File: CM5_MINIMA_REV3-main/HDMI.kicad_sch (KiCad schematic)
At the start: 7 parts, among them J501 GT-HD001B-CNNG1, U405 STMPS2151STR

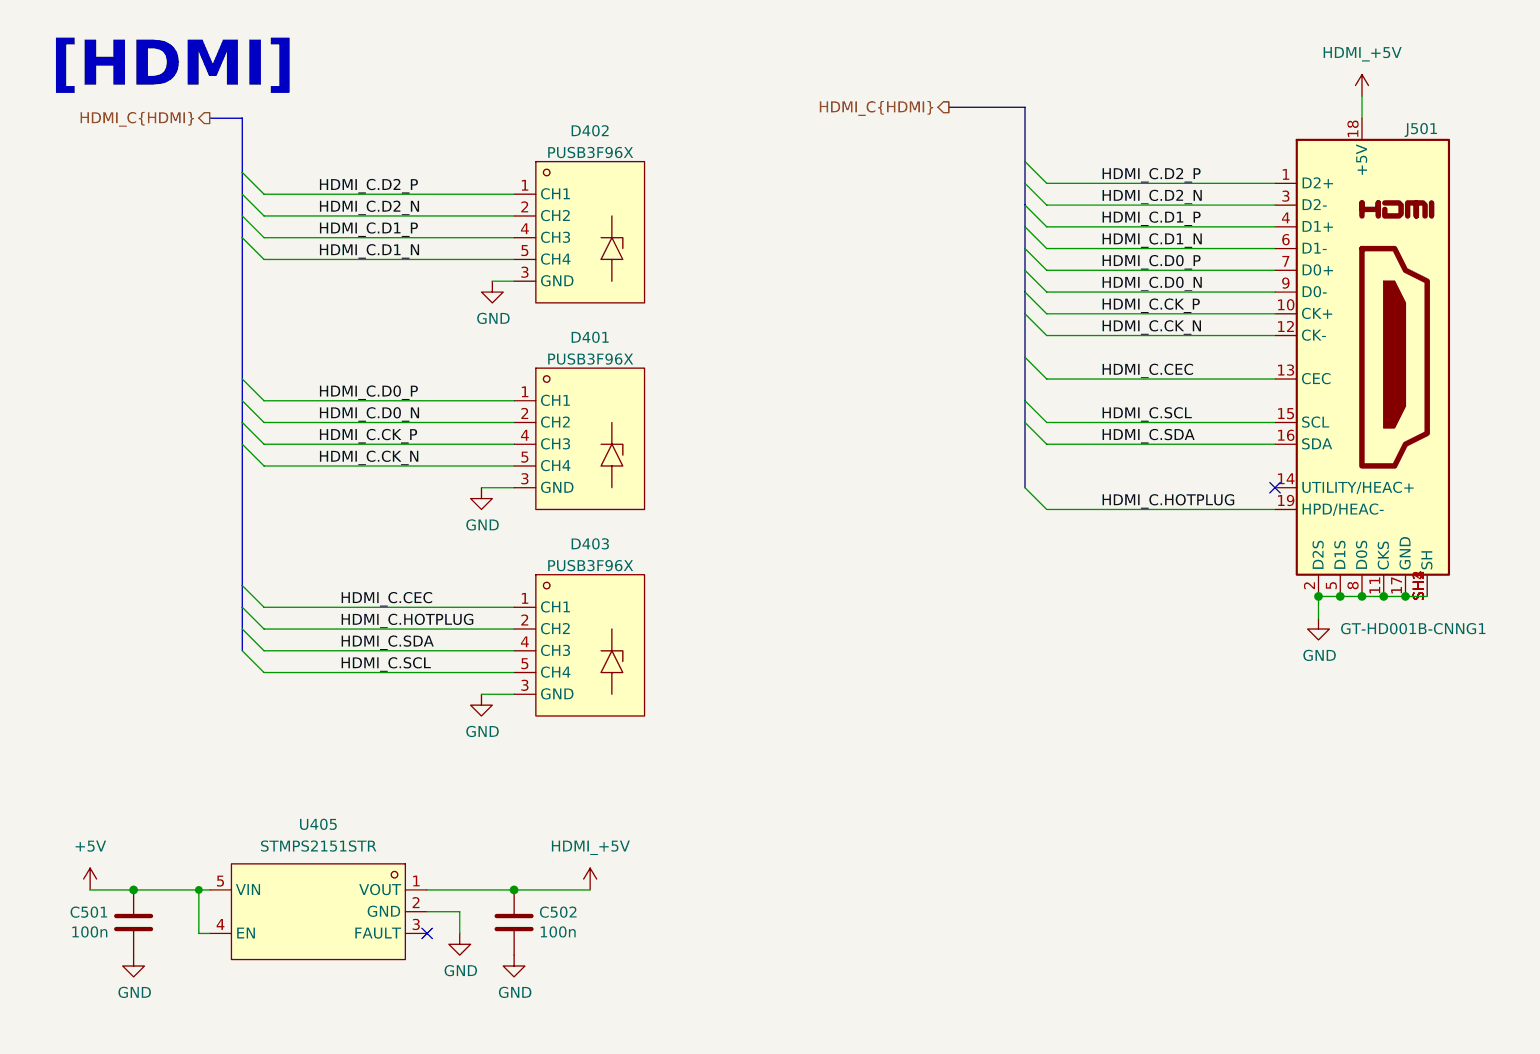
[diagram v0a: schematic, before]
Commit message: warning fix - 17 left
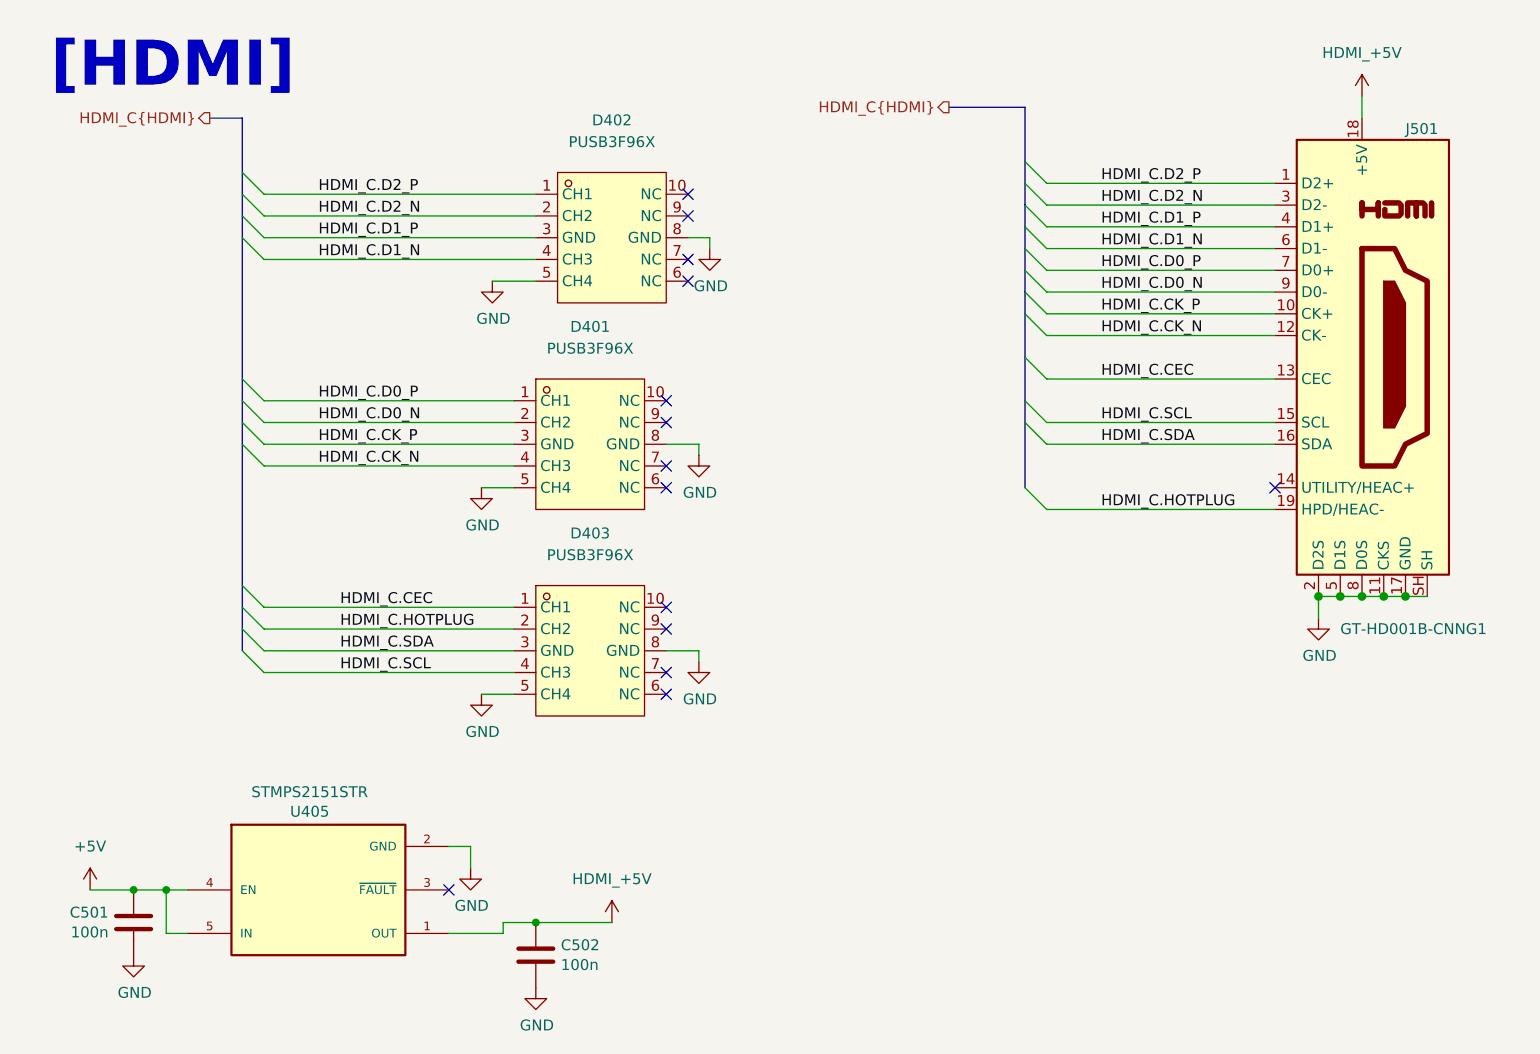
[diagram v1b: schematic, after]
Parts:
- D401, D402, D403: footprint EasyEDA:DFN2510A-10_L2.5-W1.0-P0.50-BL -> CM5_MINIMA_local:DFN2510A-10_L2.5-W1.0-P0.50-BL
- J501: footprint CM5IO:EDAC 690-019-298-412 -> CM5_MINIMA_local:EDAC 690-019-298-412; symbol CM5IO:HDMI_A_1.4 -> Connector:HDMI_A_1.4
- U405: footprint Package_TO_SOT_SMD:SOT-23-5 -> STMPS2151STR:SOT95P280X145-5N; symbol EasyEDA:STMPS2151STR -> STMPS2151STR:STMPS2151STR; Check_prices (none) -> https://www.snapeda.com/parts/STMPS2151STR/STMicroelectroni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; Description_1 (none) -> Power Switch/Driver 1:1 N-Channel 500mA SOT-23-5; DigiKey_Part_Number (none) -> 497-6934-1-ND; MANUFACTURER (none) -> STMicroelectronics; MAXIMUM_PACKAGE_HEIGHT (none) -> 1.45mm; MF (none) -> STMicroelectronics; MP (none) -> STMPS2151STR; PARTREV (none) -> 7; Package (none) -> SOT-23-5 STMicroelectronics; STANDARD (none) -> IPC-7351B; SnapEDA_Link (none) -> https://www.snapeda.com/parts/STMPS2151STR/STMicroelectroni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
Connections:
- net GND: now also D401.5 (CH4), D402.5 (CH4), D403.5 (CH4), J501.SH; no longer D401.3 (GND), D402.3 (GND), D403.3 (GND), J501.SH1 (SH), J501.SH2 (SH), J501.SH3 (SH), J501.SH4 (SH)
- net HDMI_C.CEC: no longer D403.10 (NC)
- net HDMI_C.CK_N: now also D401.4 (CH3); no longer D401.5 (CH4), D401.6 (NC)
- net HDMI_C.CK_P: now also D401.3 (GND); no longer D401.4 (CH3), D401.7 (NC)
- net HDMI_C.D0_N: no longer D401.9 (NC)
- net HDMI_C.D0_P: no longer D401.10 (NC)
- net HDMI_C.D1_N: now also D402.4 (CH3); no longer D402.5 (CH4), D402.6 (NC)
- net HDMI_C.D1_P: now also D402.3 (GND); no longer D402.4 (CH3), D402.7 (NC)
- net HDMI_C.D2_N: no longer D402.9 (NC)
- net HDMI_C.D2_P: no longer D402.10 (NC)
- net HDMI_C.HOTPLUG: no longer D403.9 (NC)
- net HDMI_C.SCL: now also D403.4 (CH3); no longer D403.5 (CH4), D403.6 (NC)
- net HDMI_C.SDA: now also D403.3 (GND); no longer D403.4 (CH3), D403.7 (NC)
- no-connect marks 2 -> 14
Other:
- moved on the sheet: C502

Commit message: warning fix - 0  in schematic
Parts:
- U405: footprint STMPS2151STR:SOT95P280X145-5N -> seeed esp32:SOT95P280X145-5N
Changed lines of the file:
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@@
 			)
 		)
-		(property "Footprint" "STMPS2151STR:SOT95P280X145-5N"
+		(property "Footprint" "seeed esp32:SOT95P280X145-5N"
 			(at 45.72 118.11 0)
 			(effects

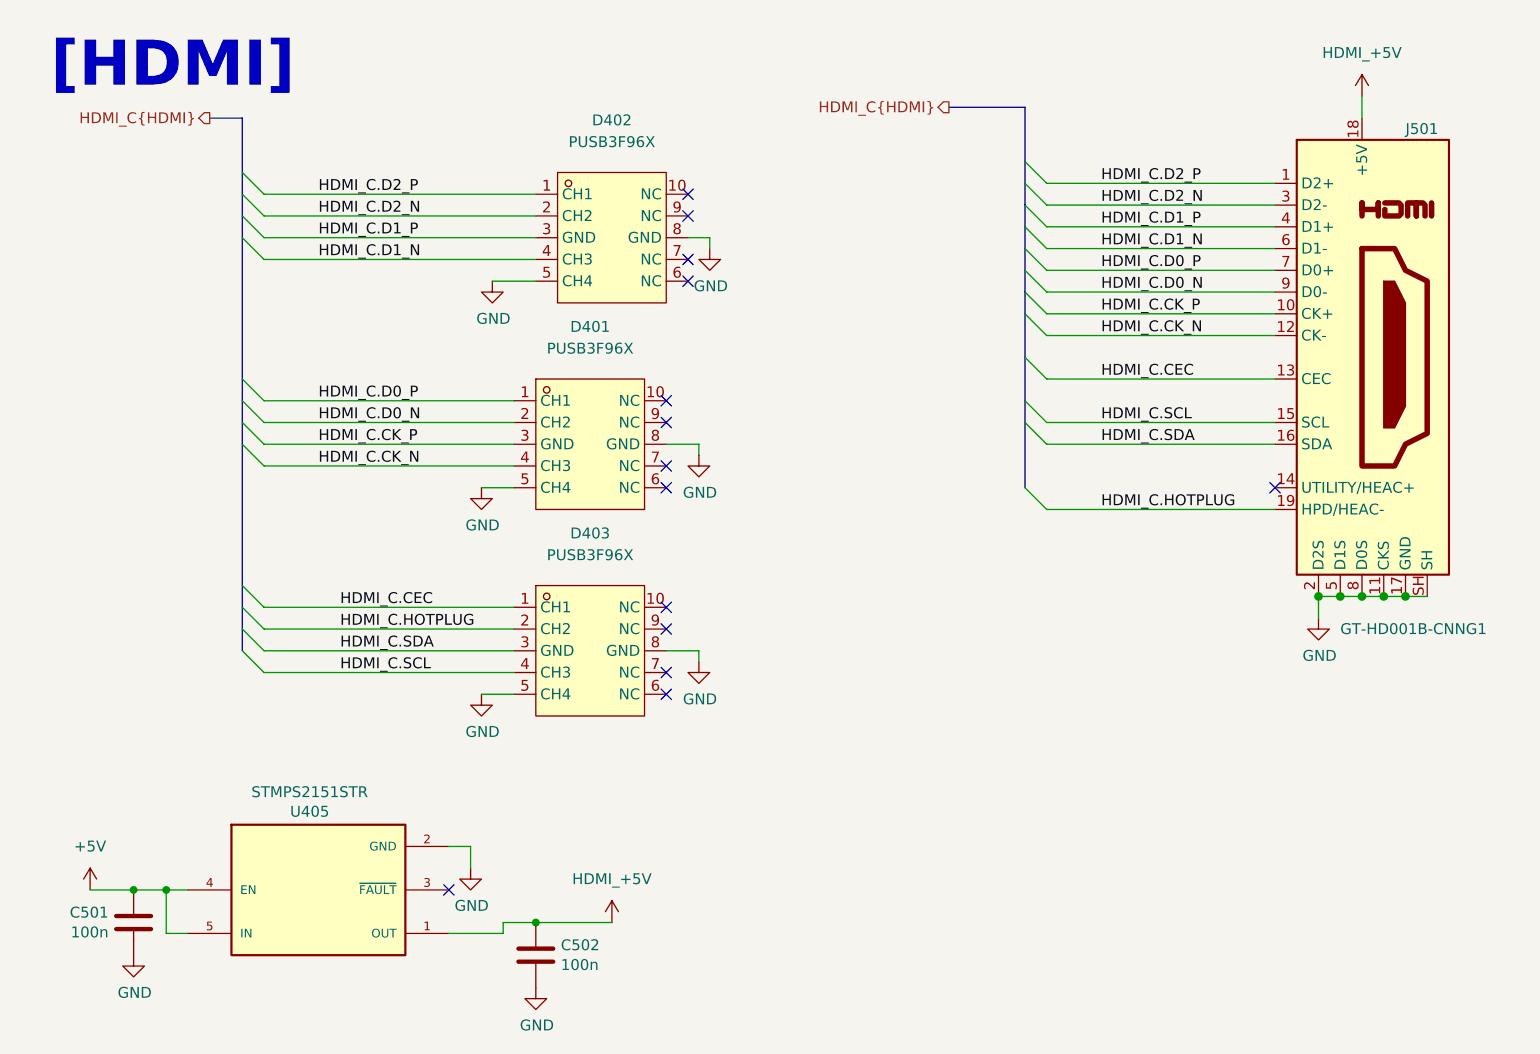
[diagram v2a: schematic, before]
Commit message: Revert CM5_MINIMA_REV3-main to pre-warning-fix state (feae2c2) - fix component mismatches
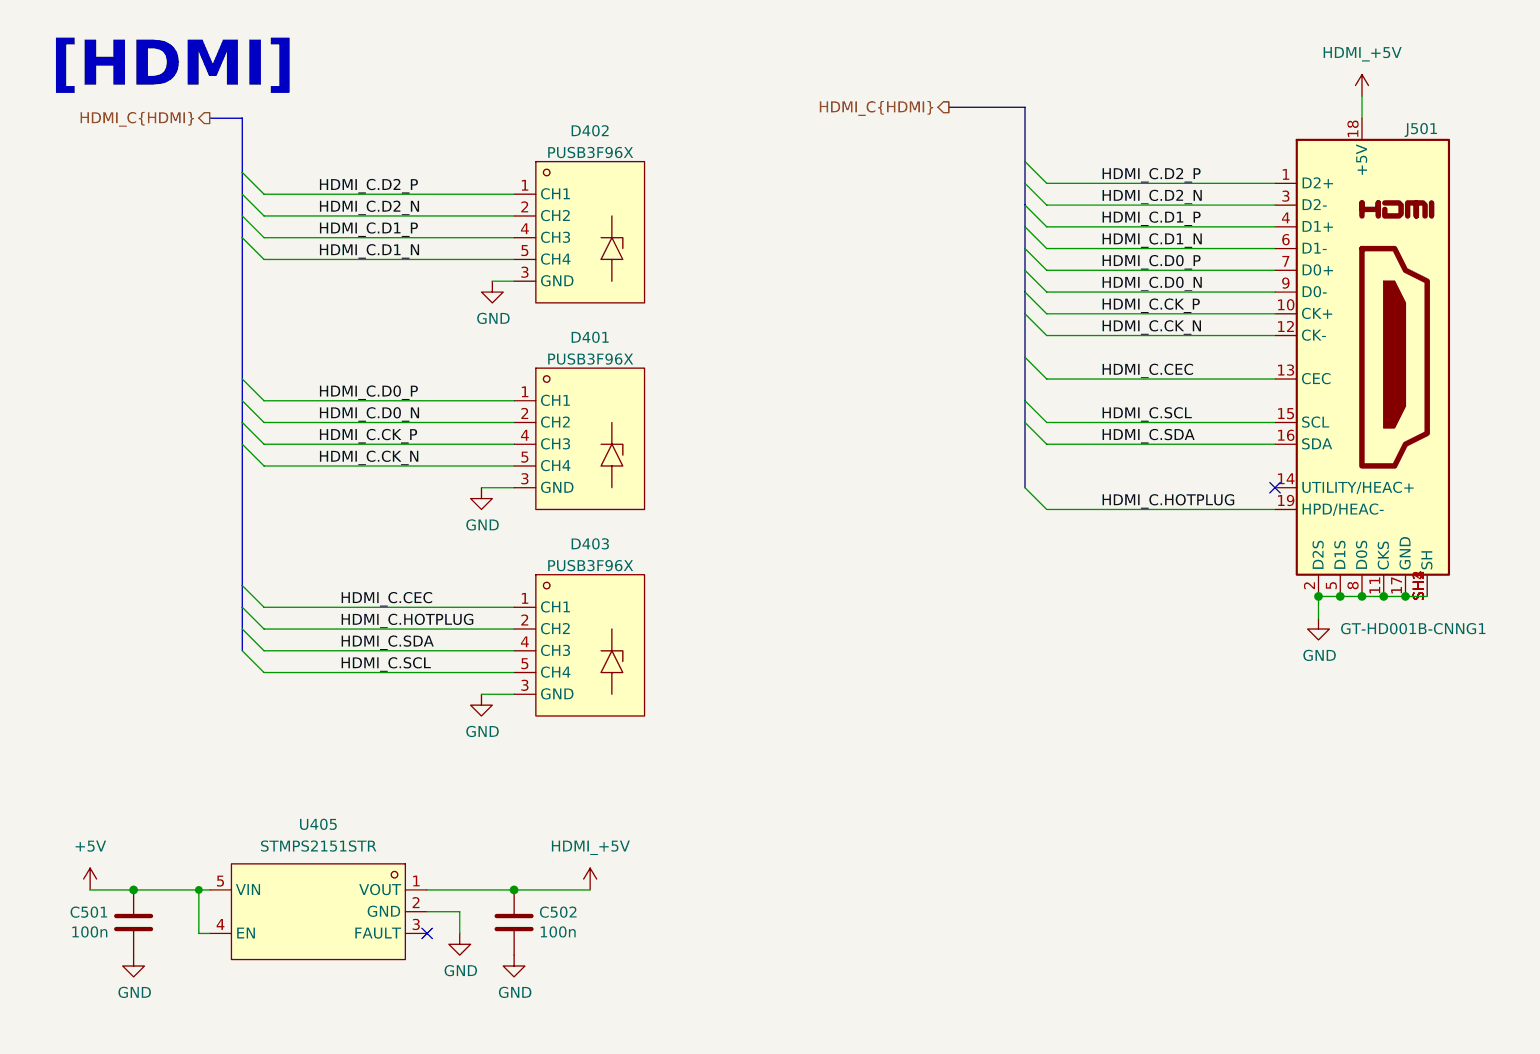
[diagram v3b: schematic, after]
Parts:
- D401, D402, D403: footprint CM5_MINIMA_local:DFN2510A-10_L2.5-W1.0-P0.50-BL -> EasyEDA:DFN2510A-10_L2.5-W1.0-P0.50-BL
- J501: footprint CM5_MINIMA_local:EDAC 690-019-298-412 -> CM5IO:EDAC 690-019-298-412; symbol Connector:HDMI_A_1.4 -> CM5IO:HDMI_A_1.4
- U405: footprint seeed esp32:SOT95P280X145-5N -> Package_TO_SOT_SMD:SOT-23-5; symbol STMPS2151STR:STMPS2151STR -> EasyEDA:STMPS2151STR; Check_prices https://www.snapeda.com/parts/STMPS2151STR/STMicroelectroni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 -> (none); Description_1 Power Switch/Driver 1:1 N-Channel 500mA SOT-23-5 -> (none); DigiKey_Part_Number 497-6934-1-ND -> (none); MANUFACTURER STMicroelectronics -> (none); MAXIMUM_PACKAGE_HEIGHT 1.45mm -> (none); MF STMicroelectronics -> (none); MP STMPS2151STR -> (none); PARTREV 7 -> (none); Package SOT-23-5 STMicroelectronics -> (none); STANDARD IPC-7351B -> (none); SnapEDA_Link https://www.snapeda.com/parts/STMPS2151STR/STMicroelectroni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 -> (none)
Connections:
- net GND: now also D401.3 (GND), D402.3 (GND), D403.3 (GND), J501.SH1 (SH), J501.SH2 (SH), J501.SH3 (SH), J501.SH4 (SH); no longer D401.5 (CH4), D402.5 (CH4), D403.5 (CH4), J501.SH
- net HDMI_C.CEC: now also D403.10 (NC)
- net HDMI_C.CK_N: now also D401.5 (CH4), D401.6 (NC); no longer D401.4 (CH3)
- net HDMI_C.CK_P: now also D401.4 (CH3), D401.7 (NC); no longer D401.3 (GND)
- net HDMI_C.D0_N: now also D401.9 (NC)
- net HDMI_C.D0_P: now also D401.10 (NC)
- net HDMI_C.D1_N: now also D402.5 (CH4), D402.6 (NC); no longer D402.4 (CH3)
- net HDMI_C.D1_P: now also D402.4 (CH3), D402.7 (NC); no longer D402.3 (GND)
- net HDMI_C.D2_N: now also D402.9 (NC)
- net HDMI_C.D2_P: now also D402.10 (NC)
- net HDMI_C.HOTPLUG: now also D403.9 (NC)
- net HDMI_C.SCL: now also D403.5 (CH4), D403.6 (NC); no longer D403.4 (CH3)
- net HDMI_C.SDA: now also D403.4 (CH3), D403.7 (NC); no longer D403.3 (GND)
- no-connect marks 14 -> 2
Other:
- moved on the sheet: C502
